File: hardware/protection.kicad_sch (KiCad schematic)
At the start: 4 parts

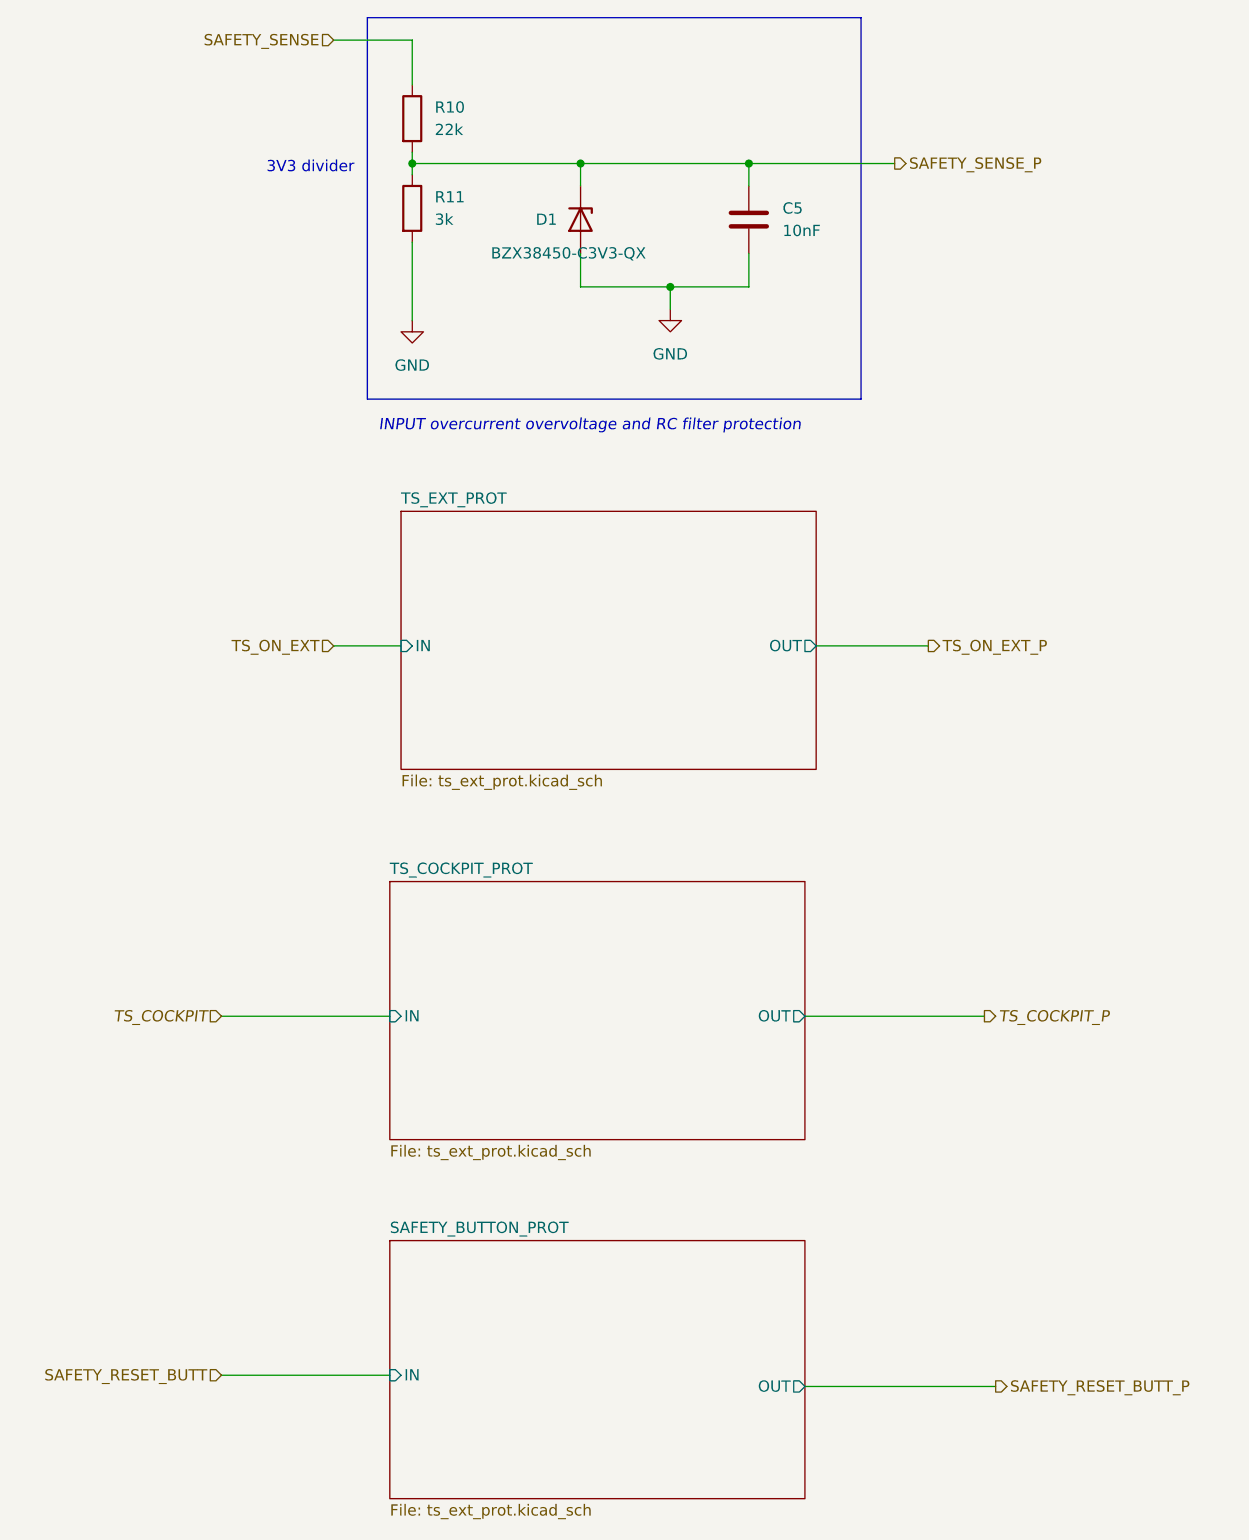
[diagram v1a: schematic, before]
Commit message: Schematic redesign for 23 rules, new pressure buffer, protection fix
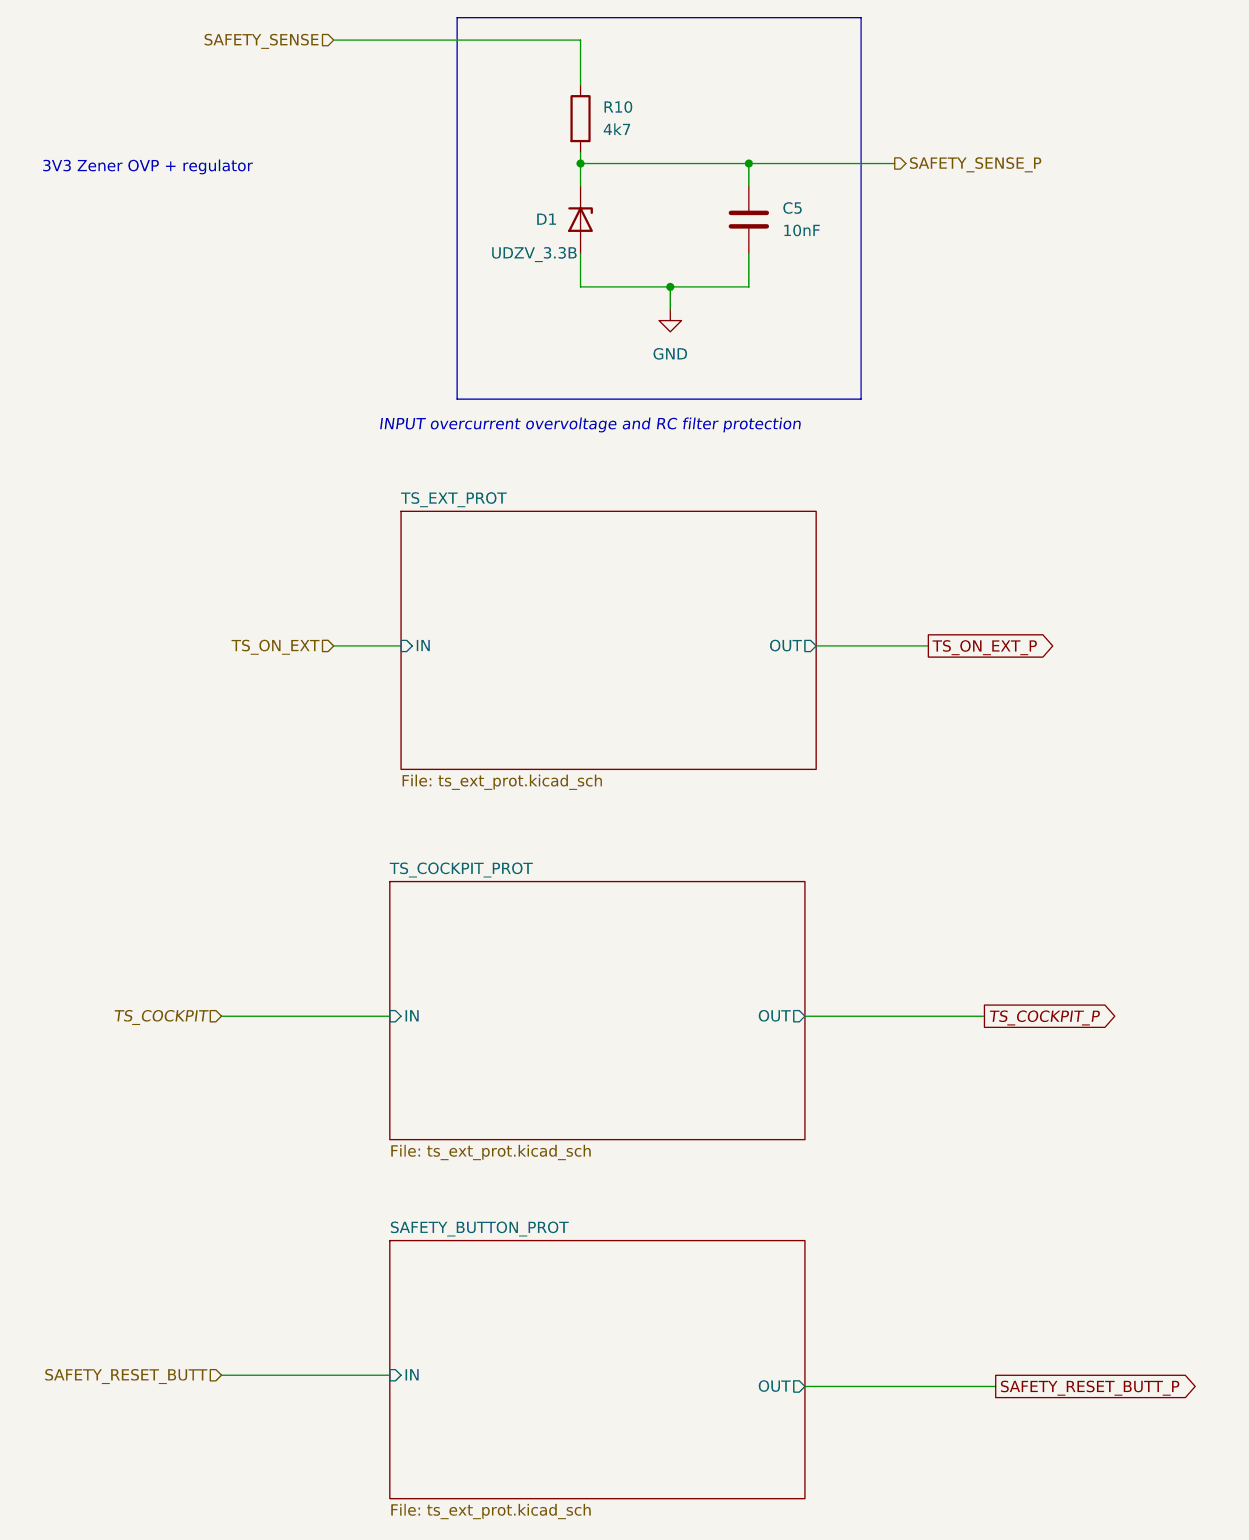
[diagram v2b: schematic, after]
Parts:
- removed R11: 3k, Resistor_SMD:R_0603_1608Metric_Pad0.98x0.95mm_HandSolder, symbol Device:R
- D1: value BZX38450-C3V3-QX -> UDZV_3.3B
- R10: value 22k -> 4k7
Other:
- note added: "3V3 Zener OVP + regulator"
- note removed: "3V3 divider"
- moved on the sheet: R10
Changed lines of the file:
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@@
   (junction (at 99.06 39.37) (diameter 0) (color 0 0 0 0)
-  )
-  (junction (at 80.01 39.37) (diameter 0) (color 0 0 0 0)
   )
   (wire (pts (xy 118.11 39.37) (xy 118.11 41.91))
@@
     (stroke (width 0) (type default))
   )
-  (polyline (pts (xy 130.81 66.04) (xy 74.93 66.04))
+  (polyline (pts (xy 130.81 66.04) (xy 85.09 66.04))
     (stroke (width 0) (type default))
   )
-  (wire (pts (xy 80.01 25.4) (xy 71.12 25.4))
+  (wire (pts (xy 99.06 25.4) (xy 71.12 25.4))
     (stroke (width 0) (type default))
   )
@@
     (stroke (width 0) (type default))
   )
-  (polyline (pts (xy 74.93 22.86) (xy 130.81 22.86))
+  (polyline (pts (xy 85.09 22.86) (xy 130.81 22.86))
     (stroke (width 0) (type default))
   )
@@
     (stroke (width 0) (type default))
   )
-  (wire (pts (xy 80.01 39.37) (xy 80.01 40.64))
-    (stroke (width 0) (type default))
-  )
   (wire (pts (xy 109.22 53.34) (xy 118.11 53.34))
     (stroke (width 0) (type default))
   )
   (wire (pts (xy 118.11 49.53) (xy 118.11 53.34))
-    (stroke (width 0) (type default))
-  )
-  (wire (pts (xy 80.01 48.26) (xy 80.01 57.15))
     (stroke (width 0) (type default))
   )
@@
     (stroke (width 0) (type default))
   )
-  (wire (pts (xy 80.01 30.48) (xy 80.01 25.4))
+  (wire (pts (xy 99.06 30.48) (xy 99.06 25.4))
     (stroke (width 0) (type default))
   )
-  (wire (pts (xy 80.01 38.1) (xy 80.01 39.37))
+  (wire (pts (xy 99.06 38.1) (xy 99.06 39.37))
     (stroke (width 0) (type default))
   )
-  (polyline (pts (xy 74.93 22.86) (xy 74.93 66.04))
+  (polyline (pts (xy 85.09 22.86) (xy 85.09 66.04))
     (stroke (width 0) (type default))
   )
-  (wire (pts (xy 80.01 39.37) (xy 99.06 39.37))
-    (stroke (width 0) (type default))
-  )
-  (text "3V3 divider\n" (at 63.5 40.64 0)
+  (text "3V3 Zener OVP + regulator\n" (at 38.1 40.64 0)
     (effects (font (size 1.27 1.27)) (justify left bottom))
   )
@@
     (at 76.2 69.85 0)
     (effects (font (size 1.27 1.27) italic) (justify left bottom))
+  )
+  (global_label "TS_COCKPIT_P" (shape output) (at 144.78 135.89 0) (fields_autoplaced)
+    (effects (font (size 1.27 1.27) italic) (justify left))
+    (property "Intersheetrefs" "${INTERSHEET_REFS}" (at 160.9299 135.89 0)
+      (effects (font (size 1.27 1.27)) (justify left) hide)
+    )
+  )
+  (global_label "SAFETY_RESET_BUTT_P" (shape output) (at 146.05 177.8 0) (fields_autoplaced)
+    (effects (font (size 1.27 1.27)) (justify left))
+    (property "Intersheetrefs" "${INTERSHEET_REFS}" (at 170.0013 177.8 0)
+      (effects (font (size 1.27 1.27)) (justify left) hide)
+    )
+  )
+  (global_label "TS_ON_EXT_P" (shape output) (at 138.43 93.98 0) (fields_autoplaced)
+    (effects (font (size 1.27 1.27)) (justify left))
+    (property "Intersheetrefs" "${INTERSHEET_REFS}" (at 153.6728 93.98 0)
+      (effects (font (size 1.27 1.27)) (justify left) hide)
+    )
   )
   (hierarchical_label "TS_COCKPIT" (shape input) (at 58.42 135.89 180) (fields_autoplaced)
@@
     (effects (font (size 1.27 1.27)) (justify right))
   )
-  (hierarchical_label "TS_ON_EXT_P" (shape output) (at 138.43 93.98 0) (fields_autoplaced)
-    (effects (font (size 1.27 1.27)) (justify left))
-  )
   (hierarchical_label "TS_ON_EXT" (shape input) (at 71.12 93.98 180) (fields_autoplaced)
     (effects (font (size 1.27 1.27)) (justify right))
   )
-  (hierarchical_label "TS_COCKPIT_P" (shape output) (at 144.78 135.89 0) (fields_autoplaced)
-    (effects (font (size 1.27 1.27) italic) (justify left))
-  )
   (hierarchical_label "SAFETY_RESET_BUTT" (shape input) (at 58.42 176.53 180) (fields_autoplaced)
     (effects (font (size 1.27 1.27)) (justify right))
-  )
-  (hierarchical_label "SAFETY_RESET_BUTT_P" (shape output) (at 146.05 177.8 0) (fields_autoplaced)
-    (effects (font (size 1.27 1.27)) (justify left))
-  )
-  (symbol (lib_id "power:GND") (at 80.01 57.15 0) (unit 1)
-    (in_bom yes) (on_board yes) (dnp no) (fields_autoplaced)
-    (property "Reference" "#PWR012" (at 80.01 63.5 0)
-      (effects (font (size 1.27 1.27)) hide)
-    )
-    (property "Value" "GND" (at 80.01 62.23 0)
-      (effects (font (size 1.27 1.27)))
-    )
-    (property "Footprint" "" (at 80.01 57.15 0)
-      (effects (font (size 1.27 1.27)) hide)
-    )
-    (property "Datasheet" "" (at 80.01 57.15 0)
-      (effects (font (size 1.27 1.27)) hide)
-    )
-    (pin "1")
-    (instances
-      (project "PUTM_DV_EBS_2023"
-        (path "/d921fbb5-521e-405d-bdec-f40195adfa1c/7da1b602-85c7-4e23-9ab2-6325d57b1abc"
-          (reference "#PWR012") (unit 1)
-        )
-      )
-    )
   )
   (symbol (lib_id "Device:C") (at 118.11 45.72 0) (unit 1)
@@
     )
   )
-  (symbol (lib_id "Device:R") (at 80.01 34.29 0) (unit 1)
+  (symbol (lib_id "Device:R") (at 99.06 34.29 0) (unit 1)
     (in_bom yes) (on_board yes) (dnp no) (fields_autoplaced)
-    (property "Reference" "R10" (at 82.55 33.0199 0)
+    (property "Reference" "R10" (at 101.6 33.0199 0)
       (effects (font (size 1.27 1.27)) (justify left))
     )
-    (property "Value" "22k" (at 82.55 35.5599 0)
+    (property "Value" "4k7" (at 101.6 35.5599 0)
       (effects (font (size 1.27 1.27)) (justify left))
     )
-    (property "Footprint" "Resistor_SMD:R_0603_1608Metric_Pad0.98x0.95mm_HandSolder" (at 78.232 34.29 90)
+    (property "Footprint" "Resistor_SMD:R_0603_1608Metric_Pad0.98x0.95mm_HandSolder" (at 97.282 34.29 90)
       (effects (font (size 1.27 1.27)) hide)
     )
-    (property "Datasheet" "~" (at 80.01 34.29 0)
+    (property "Datasheet" "~" (at 99.06 34.29 0)
       (effects (font (size 1.27 1.27)) hide)
     )
@@
     )
   )
-  (symbol (lib_id "Device:R") (at 80.01 44.45 0) (unit 1)
-    (in_bom yes) (on_board yes) (dnp no) (fields_autoplaced)
-    (property "Reference" "R11" (at 82.55 43.1799 0)
-      (effects (font (size 1.27 1.27)) (justify left))
-    )
-    (property "Value" "3k" (at 82.55 45.7199 0)
-      (effects (font (size 1.27 1.27)) (justify left))
-    )
-    (property "Footprint" "Resistor_SMD:R_0603_1608Metric_Pad0.98x0.95mm_HandSolder" (at 78.232 44.45 90)
-      (effects (font (size 1.27 1.27)) hide)
-    )
-    (property "Datasheet" "~" (at 80.01 44.45 0)
-      (effects (font (size 1.27 1.27)) hide)
-    )
-    (pin "1")
-    (pin "2")
-    (instances
-      (project "PUTM_DV_EBS_2023"
-        (path "/d921fbb5-521e-405d-bdec-f40195adfa1c/7da1b602-85c7-4e23-9ab2-6325d57b1abc"
-          (reference "R11") (unit 1)
-        )
-      )
-    )
-  )
   (symbol (lib_id "Device:D_Zener") (at 99.06 45.72 270) (unit 1)
     (in_bom yes) (on_board yes) (dnp no)
@@
       (effects (font (size 1.27 1.27)) (justify left))
     )
-    (property "Value" "BZX38450-C3V3-QX" (at 88.9 49.53 90)
+    (property "Value" "UDZV_3.3B" (at 88.9 49.53 90)
       (effects (font (size 1.27 1.27)) (justify left))
     )

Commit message: changed pcb version
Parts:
- added R11: 3k, Resistor_SMD:R_0603_1608Metric_Pad0.98x0.95mm_HandSolder, symbol Device:R
- D1: value UDZV_3.3B -> BZX38450-C3V3-QX
- R10: value 4k7 -> 22k
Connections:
- net GND: now also R11.2
- net SAFETY_SENSE_P: now also R11.1
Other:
- note added: "3V3 divider"
- note removed: "3V3 Zener OVP + regulator"
- moved on the sheet: R10
